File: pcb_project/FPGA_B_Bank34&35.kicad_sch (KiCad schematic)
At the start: 13 parts, among them U1 XC7A100T-FTG256, Y2 XLH736025.175000I

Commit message: FPGA decoupler
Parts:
- added R66: 22k, Resistor_SMD:R_0805_2012Metric_Pad1.20x1.40mm_HandSolder, symbol Device:R
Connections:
- net +3V3: now also R66.1
- net G0: now also U1.G5 (IO_L16P_T2_35); no longer U1.F2 (IO_L15P_T2_DQS_35)
- net G1: now also U1.G4 (IO_L16N_T2_35); no longer U1.E1 (IO_L15N_T2_DQS_35)
- net G2: now also U1.G2 (IO_L17P_T2_35); no longer U1.G5 (IO_L16P_T2_35)
- net G3: now also U1.G1 (IO_L17N_T2_35); no longer U1.G4 (IO_L16N_T2_35)
- net G4: now also U1.H5 (IO_L18P_T2_35); no longer U1.G2 (IO_L17P_T2_35)
- net G5: now also U1.H4 (IO_L18N_T2_35); no longer U1.G1 (IO_L17N_T2_35)
- net R0: now also U1.E5 (IO_L13N_T2_MRCC_35); no longer U1.C4 (IO_L12N_T1_MRCC_35)
- net R1: now also U1.F4 (IO_L14P_T2_SRCC_35); no longer U1.F5 (IO_L13P_T2_MRCC_35)
- net R2: now also U1.F3 (IO_L14N_T2_SRCC_35); no longer U1.E5 (IO_L13N_T2_MRCC_35)
- net R3: now also U1.F2 (IO_L15P_T2_DQS_35); no longer U1.F4 (IO_L14P_T2_SRCC_35)
- net R4: now also U1.E1 (IO_L15N_T2_DQS_35); no longer U1.F3 (IO_L14N_T2_SRCC_35)
- net OSPI CS: now reaches U1.E6 (IO_0_35)
- net OSPI CS: now also R66.2
- new net OSPI CLK: U1.F5 (IO_L13P_T2_MRCC_35)
- no-connect marks 53 -> 50

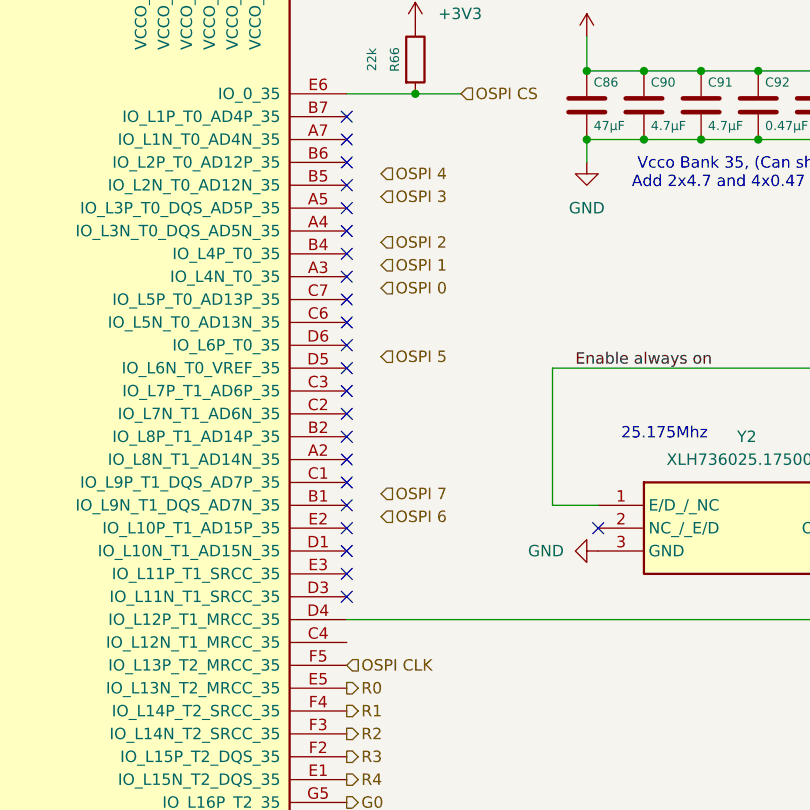
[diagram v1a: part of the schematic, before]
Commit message: Add another SRAM
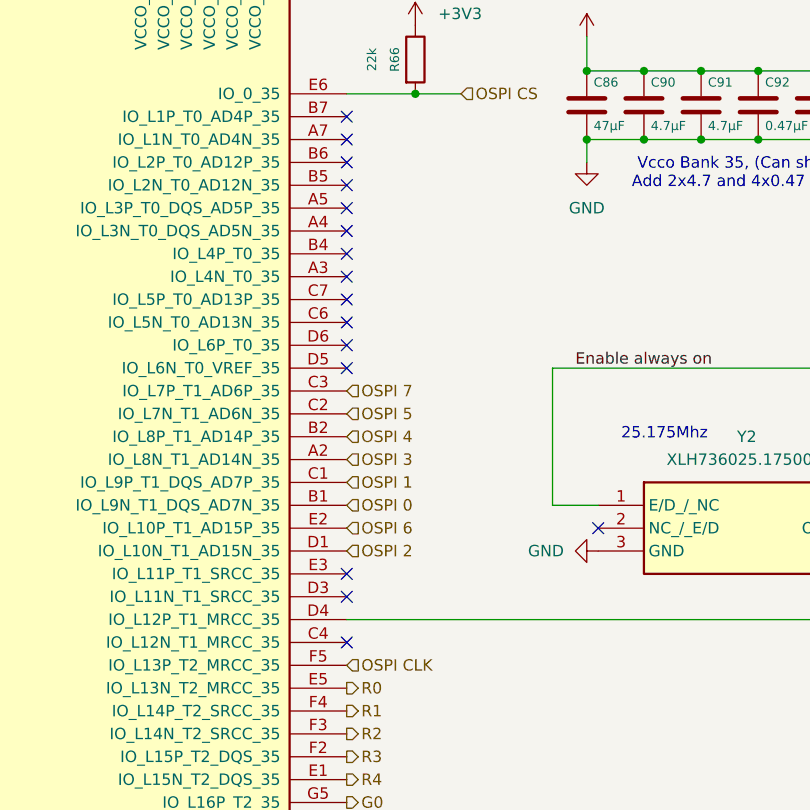
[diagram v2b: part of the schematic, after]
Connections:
- net OSPI 0: now also U1.B1 (IO_L9N_T1_DQS_AD7N_35)
- net OSPI 1: now also U1.C1 (IO_L9P_T1_DQS_AD7P_35)
- net OSPI 2: now also U1.D1 (IO_L10N_T1_AD15N_35)
- net OSPI 3: now also U1.A2 (IO_L8N_T1_AD14N_35)
- net OSPI 4: now also U1.B2 (IO_L8P_T1_AD14P_35)
- net OSPI 5: now also U1.C2 (IO_L7N_T1_AD6N_35)
- net OSPI 6: now also U1.E2 (IO_L10P_T1_AD15P_35)
- net OSPI 7: now also U1.C3 (IO_L7P_T1_AD6P_35)
- no-connect marks 50 -> 43
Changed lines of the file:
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@@
-	)
-	(no_connect
-		(at 196.85 80.01)
 	)
 	(no_connect
@@
 	)
 	(no_connect
-		(at 196.85 85.09)
-	)
-	(no_connect
 		(at 95.25 82.55)
 	)
@@
 	)
 	(no_connect
-		(at 196.85 74.93)
-	)
-	(no_connect
-		(at 196.85 69.85)
-	)
-	(no_connect
-		(at 196.85 67.31)
-	)
-	(no_connect
 		(at 196.85 87.63)
 	)
@@
 	)
 	(no_connect
-		(at 196.85 72.39)
-	)
-	(no_connect
 		(at 196.85 133.35)
 	)
 	(no_connect
-		(at 196.85 77.47)
-	)
-	(no_connect
 		(at 95.25 36.83)
 	)
@@
 	)
 	(no_connect
-		(at 196.85 82.55)
+		(at 196.85 95.25)
 	)
 	(no_connect
@@
 	(hierarchical_label "OSPI 2"
 		(shape input)
-		(at 200.66 50.8 0)
+		(at 196.85 85.09 0)
 		(effects
 			(font
@@
 	(hierarchical_label "OSPI 0"
 		(shape input)
-		(at 200.66 55.88 0)
+		(at 196.85 80.01 0)
 		(effects
 			(font
@@
 	(hierarchical_label "OSPI 6"
 		(shape input)
-		(at 200.66 81.28 0)
+		(at 196.85 82.55 0)
 		(effects
 			(font
@@
 	(hierarchical_label "OSPI 3"
 		(shape input)
-		(at 200.66 45.72 0)
+		(at 196.85 74.93 0)
 		(effects
 			(font
@@
 	(hierarchical_label "OSPI 5"
 		(shape input)
-		(at 200.66 63.5 0)
+		(at 196.85 69.85 0)
 		(effects
 			(font
@@
 	(hierarchical_label "OSPI 7"
 		(shape input)
-		(at 200.66 78.74 0)
+		(at 196.85 67.31 0)
 		(effects
 			(font
@@
 	(hierarchical_label "OSPI 4"
 		(shape input)
-		(at 200.66 43.18 0)
+		(at 196.85 72.39 0)
 		(effects
 			(font
@@
 	(hierarchical_label "OSPI 1"
 		(shape input)
-		(at 200.66 53.34 0)
-		(effects
-			(font
+		(at 196.85 77.47 0)
+		(effects
+			(font

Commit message: Initial FPGA ballout and vga
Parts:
- C92, C93, C94, C95: footprint Capacitor_SMD:C_0805_2012Metric_Pad1.18x1.45mm_HandSolder -> Capacitor_SMD:C_0603_1608Metric_Pad1.08x0.95mm_HandSolder
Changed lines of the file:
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@@
 			)
 		)
-		(property "Footprint" "Capacitor_SMD:C_0805_2012Metric_Pad1.18x1.45mm_HandSolder"
+		(property "Footprint" "Capacitor_SMD:C_0603_1608Metric_Pad1.08x0.95mm_HandSolder"
 			(at 243.5352 39.37 0)
 			(effects
@@
 			)
 		)
-		(property "Footprint" "Capacitor_SMD:C_0805_2012Metric_Pad1.18x1.45mm_HandSolder"
+		(property "Footprint" "Capacitor_SMD:C_0603_1608Metric_Pad1.08x0.95mm_HandSolder"
 			(at 262.5852 39.37 0)
 			(effects
@@
 			)
 		)
-		(property "Footprint" "Capacitor_SMD:C_0805_2012Metric_Pad1.18x1.45mm_HandSolder"
+		(property "Footprint" "Capacitor_SMD:C_0603_1608Metric_Pad1.08x0.95mm_HandSolder"
 			(at 256.2352 39.37 0)
 			(effects
@@
 			)
 		)
-		(property "Footprint" "Capacitor_SMD:C_0805_2012Metric_Pad1.18x1.45mm_HandSolder"
+		(property "Footprint" "Capacitor_SMD:C_0603_1608Metric_Pad1.08x0.95mm_HandSolder"
 			(at 249.8852 39.37 0)
 			(effects

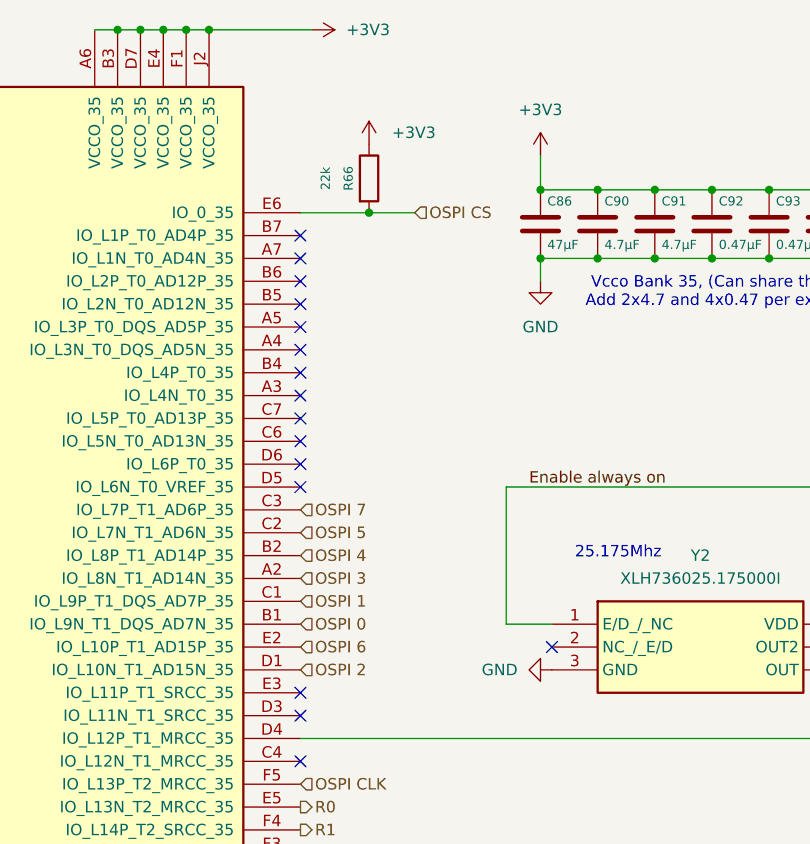
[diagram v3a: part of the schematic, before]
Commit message: Change FPGA OSPI pins and connect to MCU only top layer
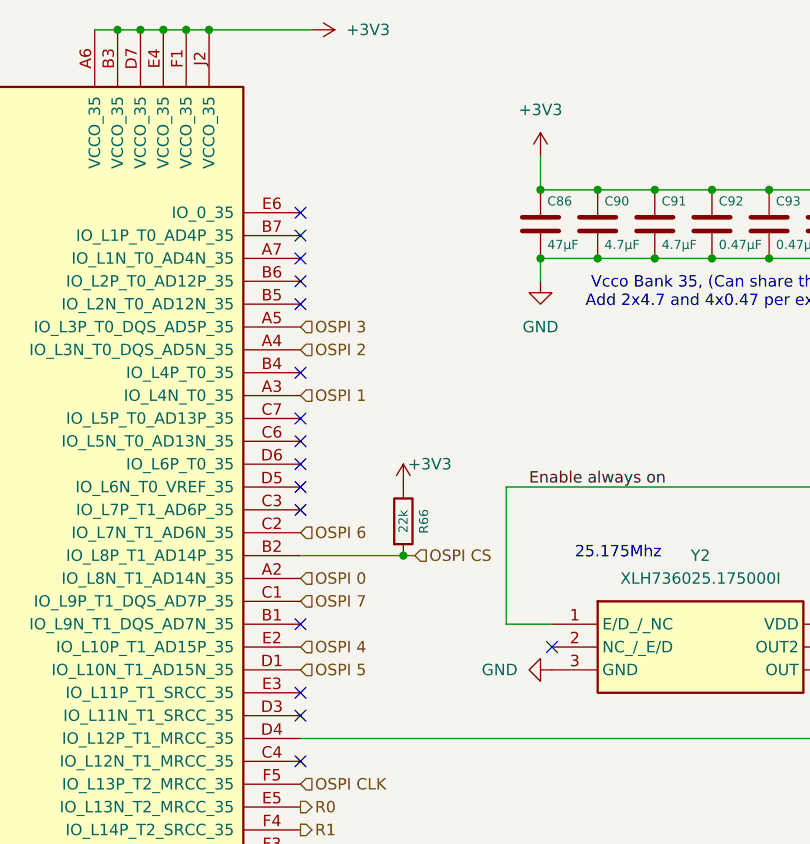
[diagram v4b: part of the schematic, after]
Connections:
- net OSPI 0: now also U1.A2 (IO_L8N_T1_AD14N_35); no longer U1.B1 (IO_L9N_T1_DQS_AD7N_35)
- net OSPI 1: now also U1.A3 (IO_L4N_T0_35); no longer U1.C1 (IO_L9P_T1_DQS_AD7P_35)
- net OSPI 2: now also U1.A4 (IO_L3N_T0_DQS_AD5N_35); no longer U1.D1 (IO_L10N_T1_AD15N_35)
- net OSPI 3: now also U1.A5 (IO_L3P_T0_DQS_AD5P_35); no longer U1.A2 (IO_L8N_T1_AD14N_35)
- net OSPI 4: now also U1.E2 (IO_L10P_T1_AD15P_35); no longer U1.B2 (IO_L8P_T1_AD14P_35)
- net OSPI 5: now also U1.D1 (IO_L10N_T1_AD15N_35); no longer U1.C2 (IO_L7N_T1_AD6N_35)
- net OSPI 6: now also U1.C2 (IO_L7N_T1_AD6N_35); no longer U1.E2 (IO_L10P_T1_AD15P_35)
- net OSPI 7: now also U1.C1 (IO_L9P_T1_DQS_AD7P_35); no longer U1.C3 (IO_L7P_T1_AD6P_35)
- net OSPI CS: now also U1.B2 (IO_L8P_T1_AD14P_35); no longer U1.E6 (IO_0_35)
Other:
- moved on the sheet: R66
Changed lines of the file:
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@@
-	)
-	(junction
-		(at 204.47 34.29)
-		(diameter 0)
-		(color 0 0 0 0)
 	)
 	(junction
@@
 		(color 0 0 0 0)
 	)
+	(junction
+		(at 208.28 72.39)
+		(diameter 0)
+		(color 0 0 0 0)
+	)
 	(no_connect
 		(at 196.85 62.23)
@@
 	)
 	(no_connect
+		(at 196.85 80.01)
+	)
+	(no_connect
 		(at 95.25 54.61)
 	)
@@
 	)
 	(no_connect
-		(at 196.85 54.61)
-	)
-	(no_connect
 		(at 196.85 90.17)
 	)
@@
 	)
 	(no_connect
+		(at 196.85 67.31)
+	)
+	(no_connect
 		(at 95.25 36.83)
 	)
 	(no_connect
-		(at 196.85 46.99)
-	)
-	(no_connect
 		(at 196.85 140.97)
 	)
@@
 	)
 	(no_connect
-		(at 196.85 49.53)
-	)
-	(no_connect
 		(at 196.85 128.27)
 	)
@@
 	)
 	(no_connect
+		(at 196.85 34.29)
+	)
+	(no_connect
 		(at 224.79 82.55)
 	)
@@
 	(wire
 		(pts
-			(xy 196.85 34.29) (xy 204.47 34.29)
-		)
-		(stroke
-			(width 0)
-			(type default)
-		)
-	)
-	(wire
-		(pts
-			(xy 204.47 34.29) (xy 209.55 34.29)
+			(xy 208.28 72.39) (xy 209.55 72.39)
 		)
 		(stroke
@@
 		(pts
 			(xy 242.57 31.75) (xy 248.92 31.75)
+		)
+		(stroke
+			(width 0)
+			(type default)
+		)
+	)
+	(wire
+		(pts
+			(xy 196.85 72.39) (xy 208.28 72.39)
 		)
 		(stroke
@@
 	(hierarchical_label "OSPI 2"
 		(shape input)
-		(at 196.85 85.09 0)
+		(at 196.85 49.53 0)
 		(effects
 			(font
@@
 	(hierarchical_label "OSPI 0"
 		(shape input)
-		(at 196.85 80.01 0)
+		(at 196.85 74.93 0)
 		(effects
 			(font
@@
 	(hierarchical_label "OSPI 6"
 		(shape input)
-		(at 196.85 82.55 0)
+		(at 196.85 69.85 0)
 		(effects
 			(font
@@
 	(hierarchical_label "OSPI 3"
 		(shape input)
-		(at 196.85 74.93 0)
+		(at 196.85 46.99 0)
 		(effects
 			(font
@@
 	(hierarchical_label "OSPI CS"
 		(shape input)
-		(at 209.55 34.29 0)
+		(at 209.55 72.39 0)
 		(effects
 			(font
@@
 	(hierarchical_label "OSPI 5"
 		(shape input)
-		(at 196.85 69.85 0)
+		(at 196.85 85.09 0)
 		(effects
 			(font
@@
 	(hierarchical_label "OSPI 7"
 		(shape input)
-		(at 196.85 67.31 0)
+		(at 196.85 77.47 0)
 		(effects
 			(font
@@
 	(hierarchical_label "OSPI 4"
 		(shape input)
-		(at 196.85 72.39 0)
+		(at 196.85 82.55 0)
 		(effects
 			(font
@@
 	(hierarchical_label "OSPI 1"
 		(shape input)
-		(at 196.85 77.47 0)
+		(at 196.85 54.61 0)
 		(effects
 			(font
@@
 	(symbol
 		(lib_id "Device:R")
-		(at 204.47 30.48 0)
+		(at 208.28 68.58 0)
 		(unit 1)
 		(exclude_from_sim no)
@@
 		(dnp no)
 		(property "Reference" "R66"
-			(at 202.184 30.48 90)
+			(at 210.566 68.58 90)
 			(effects
 				(font
@@
 		)
 		(property "Value" "22k"
-			(at 199.644 30.48 90)
+			(at 208.28 68.58 90)
 			(effects
 				(font
@@
 		)
 		(property "Footprint" "Resistor_SMD:R_0805_2012Metric_Pad1.20x1.40mm_HandSolder"
-			(at 202.692 30.48 90)
+			(at 206.502 68.58 90)
 			(effects
 				(font
@@
 		)
 		(property "Datasheet" "~"
-			(at 204.47 30.48 0)
+			(at 208.28 68.58 0)
 			(effects
 				(font
@@
 		)
 		(property "Description" "Resistor"
-			(at 204.47 30.48 0)
+			(at 208.28 68.58 0)
 			(effects
 				(font
@@
 	(symbol
 		(lib_id "power:+3V3")
-		(at 204.47 26.67 0)
+		(at 208.28 64.77 0)
 		(unit 1)
 		(exclude_from_sim no)
@@
 		(on_board yes)
 		(dnp no)
-		(fields_autoplaced yes)
 		(property "Reference" "#PWR091"
-			(at 204.47 30.48 0)
+			(at 208.28 68.58 0)
 			(effects
 				(font
@@
 		)
 		(property "Value" "+3V3"
-			(at 207.01 25.3999 0)
+			(at 208.788 62.23 0)
 			(effects
 				(font
@@
 		)
 		(property "Footprint" ""
-			(at 204.47 26.67 0)
+			(at 208.28 64.77 0)
 			(effects
 				(font
@@
 		)
 		(property "Datasheet" ""
-			(at 204.47 26.67 0)
+			(at 208.28 64.77 0)
 			(effects
 				(font
@@
 		)
 		(property "Description" "Power symbol creates a global label with name \"+3V3\""
-			(at 204.47 26.67 0)
-			(effects
-				(font
+			(at 208.28 64.77 0)
+			(effects
+				(font

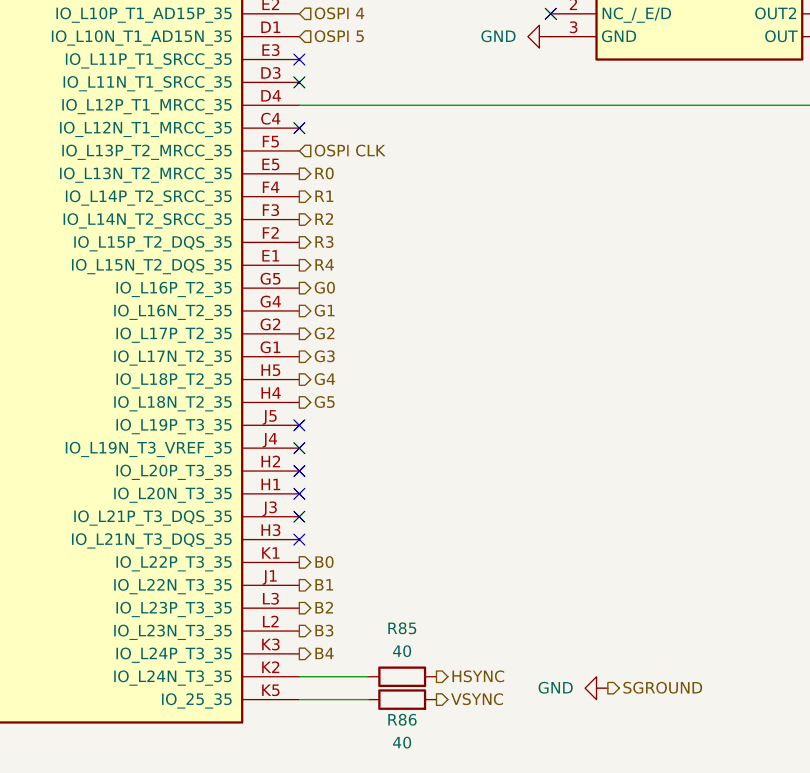
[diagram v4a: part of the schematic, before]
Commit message: VGA Layout in copy
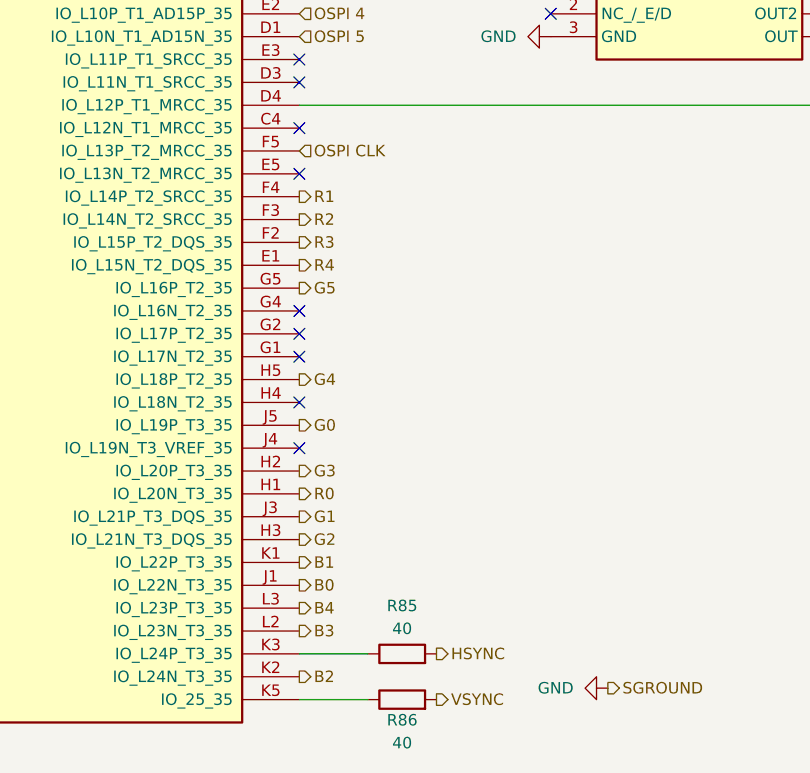
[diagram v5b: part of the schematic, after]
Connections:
- net B0: now also U1.J1 (IO_L22N_T3_35); no longer U1.K1 (IO_L22P_T3_35)
- net B1: now also U1.K1 (IO_L22P_T3_35); no longer U1.J1 (IO_L22N_T3_35)
- net B2: now also U1.K2 (IO_L24N_T3_35); no longer U1.L3 (IO_L23P_T3_35)
- net B4: now also U1.L3 (IO_L23P_T3_35); no longer U1.K3 (IO_L24P_T3_35)
- net G0: now also U1.J5 (IO_L19P_T3_35); no longer U1.G5 (IO_L16P_T2_35)
- net G1: now also U1.J3 (IO_L21P_T3_DQS_35); no longer U1.G4 (IO_L16N_T2_35)
- net G2: now also U1.H3 (IO_L21N_T3_DQS_35); no longer U1.G2 (IO_L17P_T2_35)
- net G3: now also U1.H2 (IO_L20P_T3_35); no longer U1.G1 (IO_L17N_T2_35)
- net G5: now also U1.G5 (IO_L16P_T2_35); no longer U1.H4 (IO_L18N_T2_35)
- net R0: now also U1.H1 (IO_L20N_T3_35); no longer U1.E5 (IO_L13N_T2_MRCC_35)
- net at R85.1: now also U1.K3 (IO_L24P_T3_35); no longer U1.K2 (IO_L24N_T3_35)
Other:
- moved on the sheet: R85
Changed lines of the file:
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@@
+	)
+	(no_connect
+		(at 196.85 118.11)
 	)
 	(no_connect
@@
 	)
 	(no_connect
+		(at 196.85 125.73)
+	)
+	(no_connect
 		(at 95.25 46.99)
 	)
@@
 	)
 	(no_connect
+		(at 196.85 100.33)
+	)
+	(no_connect
 		(at 196.85 57.15)
 	)
@@
 	)
 	(no_connect
-		(at 196.85 133.35)
+		(at 196.85 120.65)
 	)
 	(no_connect
@@
 	)
 	(no_connect
-		(at 196.85 140.97)
-	)
-	(no_connect
 		(at 196.85 130.81)
 	)
@@
 	)
 	(no_connect
-		(at 196.85 128.27)
-	)
-	(no_connect
 		(at 196.85 64.77)
 	)
 	(no_connect
-		(at 196.85 135.89)
-	)
-	(no_connect
 		(at 95.25 72.39)
 	)
@@
 	)
 	(no_connect
+		(at 196.85 115.57)
+	)
+	(no_connect
 		(at 95.25 49.53)
 	)
@@
 	)
 	(no_connect
-		(at 196.85 138.43)
-	)
-	(no_connect
 		(at 95.25 44.45)
 	)
@@
 	(wire
 		(pts
-			(xy 196.85 156.21) (xy 204.47 156.21)
+			(xy 196.85 153.67) (xy 204.47 153.67)
 		)
 		(stroke
@@
 	(hierarchical_label "B2"
 		(shape output)
-		(at 196.85 148.59 0)
+		(at 196.85 156.21 0)
 		(effects
 			(font
@@
 	(hierarchical_label "G3"
 		(shape output)
-		(at 196.85 120.65 0)
+		(at 196.85 133.35 0)
 		(effects
 			(font
@@
 	(hierarchical_label "G0"
 		(shape output)
-		(at 196.85 113.03 0)
+		(at 196.85 128.27 0)
 		(effects
 			(font
@@
 	(hierarchical_label "B4"
 		(shape output)
-		(at 196.85 153.67 0)
+		(at 196.85 148.59 0)
 		(effects
 			(font
@@
 	(hierarchical_label "B1"
 		(shape output)
-		(at 196.85 146.05 0)
+		(at 196.85 143.51 0)
 		(effects
 			(font
@@
 	(hierarchical_label "G1"
 		(shape output)
-		(at 196.85 115.57 0)
+		(at 196.85 138.43 0)
 		(effects
 			(font
@@
 	(hierarchical_label "G5"
 		(shape output)
-		(at 196.85 125.73 0)
+		(at 196.85 113.03 0)
 		(effects
 			(font
@@
 	(hierarchical_label "R0"
 		(shape output)
-		(at 196.85 100.33 0)
+		(at 196.85 135.89 0)
 		(effects
 			(font
@@
 	(hierarchical_label "G2"
 		(shape output)
-		(at 196.85 118.11 0)
+		(at 196.85 140.97 0)
 		(effects
 			(font
@@
 	(hierarchical_label "HSYNC"
 		(shape output)
-		(at 212.09 156.21 0)
+		(at 212.09 153.67 0)
 		(effects
 			(font
@@
 	(hierarchical_label "B0"
 		(shape output)
-		(at 196.85 143.51 0)
+		(at 196.85 146.05 0)
 		(effects
 			(font
@@
 	(symbol
 		(lib_id "Device:R")
-		(at 208.28 156.21 90)
+		(at 208.28 153.67 90)
 		(unit 1)
 		(exclude_from_sim no)
@@
 		(dnp no)
 		(property "Reference" "R85"
+			(at 208.28 148.336 90)
+			(effects
+				(font
+					(size 1.27 1.27)
+				)
+			)
+		)
+		(property "Value" "40"
 			(at 208.28 150.876 90)
 			(effects
@@
 			)
 		)
-		(property "Value" "40"
-			(at 208.28 153.416 90)
-			(effects
-				(font
-					(size 1.27 1.27)
-				)
-			)
-		)
 		(property "Footprint" "Resistor_SMD:R_0805_2012Metric_Pad1.20x1.40mm_HandSolder"
-			(at 208.28 157.988 90)
+			(at 208.28 155.448 90)
 			(effects
 				(font
@@
 		)
 		(property "Datasheet" "~"
-			(at 208.28 156.21 0)
+			(at 208.28 153.67 0)
 			(effects
 				(font
@@
 		)
 		(property "Description" "Resistor"
-			(at 208.28 156.21 0)
-			(effects
-				(font
+			(at 208.28 153.67 0)
+			(effects
+				(font
